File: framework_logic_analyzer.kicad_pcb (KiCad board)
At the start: 4 copper layers, 26 x 30 mm, 93 parts, among them IC1 TXU0104QWBQARQ1, IC2 TXU0104QWBQARQ1, IC3 TXU0104QWBQARQ1, IC4 TXU0104QWBQARQ1, IC5 CYUSB3014-BZXC, J1 Conn_02x08_Odd_Even, J2 Conn_02x08_Odd_Even, J3 Conn_ARM_JTAG_SWD_10, P1 USB_C_Plug, Q1 MMBT3904, Q2 MMBT3904, Q3 MMBT3904, U1 NCP360SNT1G, U2 WE-TVS-82400102, U3 AP2112K-3.3, U4 SC189CSKTRT, U5 M24M02-DR, Y1 19.200 MHz

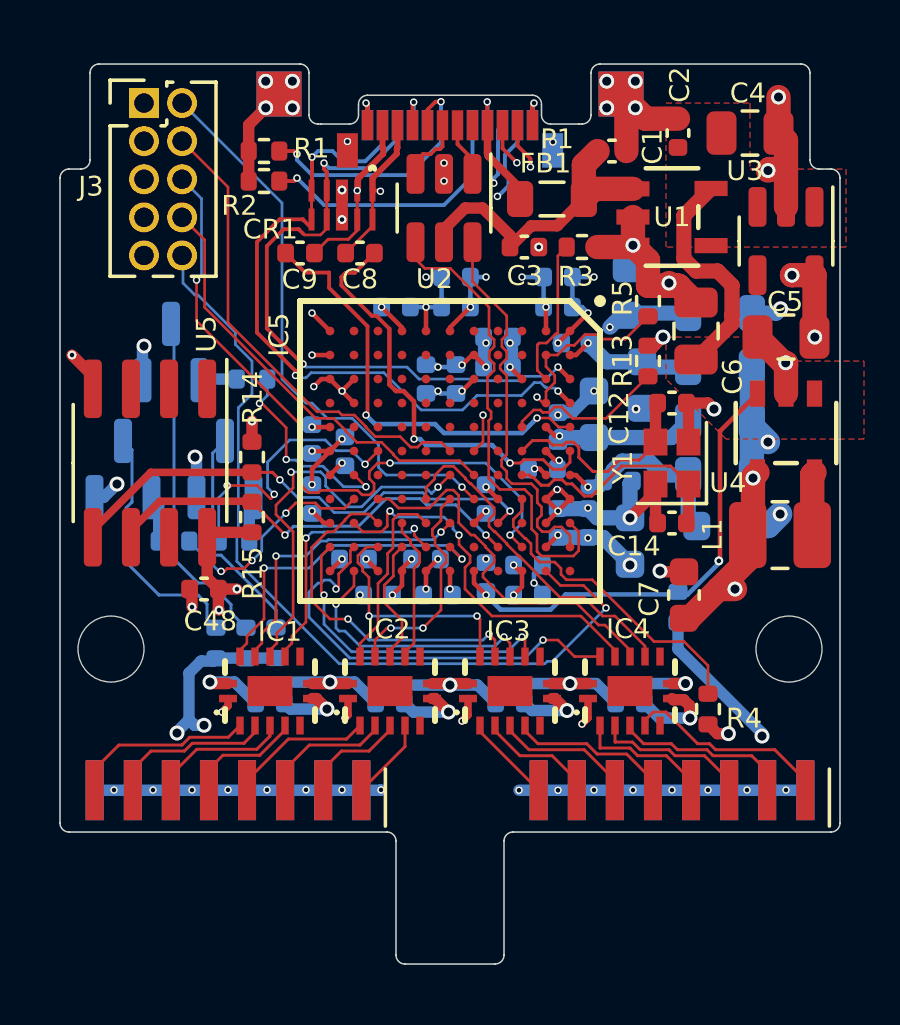
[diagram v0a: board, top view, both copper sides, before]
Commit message: update to kicad 9
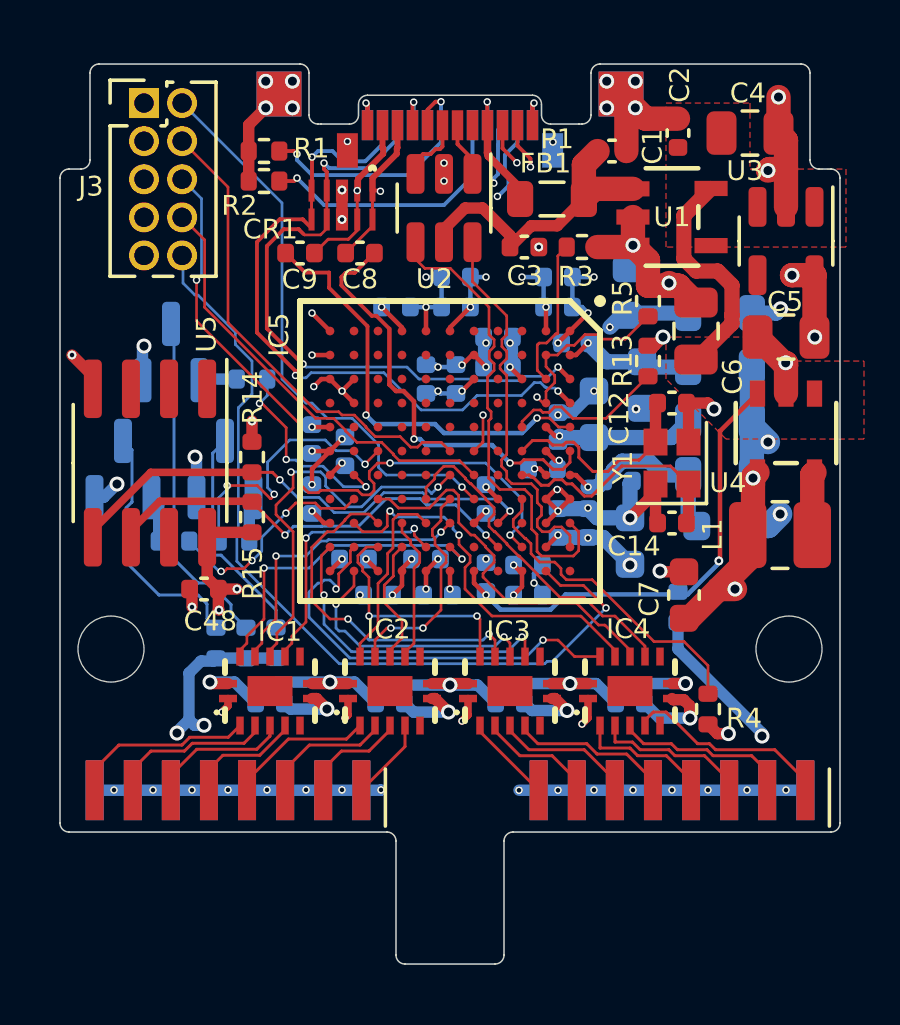
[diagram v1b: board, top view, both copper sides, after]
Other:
- outline, holes or cut-outs redrawn

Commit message: begin big refactor
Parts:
- removed J1, J2: Conn_02x08_Odd_Even, 20021311-00016T4LF:20021311-00016T4LF
- removed TP2, TP3, TP4: TestPoint, TestPoint:TestPoint_Pad_1.5x1.5mm
- added C11: 100n, Capacitor_SMD:C_0402_1005Metric, F.Cu at (154.7, 92.6)
- added C49: 100n, Capacitor_SMD:C_0402_1005Metric, F.Cu at (139.7, 92.6)
- added C50: 100n, Capacitor_SMD:C_0402_1005Metric, F.Cu at (111.7, 92.6)
- added C51: 100n, Capacitor_SMD:C_0402_1005Metric, F.Cu at (126.7, 92.6)
- added C52: 10n, Capacitor_SMD:C_0402_1005Metric, F.Cu at (110.7, 92.6)
- added C53: 10n, Capacitor_SMD:C_0402_1005Metric, F.Cu at (124.7, 92.6)
- added C54: 10n, Capacitor_SMD:C_0402_1005Metric, F.Cu at (141.7, 92.6)
- added C55: 10n, Capacitor_SMD:C_0402_1005Metric, F.Cu at (156.7, 92.6)
- added C56: 10n, Capacitor_SMD:C_0402_1005Metric, F.Cu at (156.3, 90.2)
- added C57: 10n, Capacitor_SMD:C_0402_1005Metric, F.Cu at (141.3, 89.2)
- added C58: 10n, Capacitor_SMD:C_0402_1005Metric, F.Cu at (126.3, 89.2)
- added C59: 10n, Capacitor_SMD:C_0402_1005Metric, F.Cu at (111.3, 90.2)
- added C60: 1n, Capacitor_SMD:C_0402_1005Metric, F.Cu at (126.3, 91.2)
- added C61: 1n, Capacitor_SMD:C_0402_1005Metric, F.Cu at (111.3, 91.2)
- added C62: 1n, Capacitor_SMD:C_0402_1005Metric, F.Cu at (141.3, 91.2)
- added C63: 1n, Capacitor_SMD:C_0402_1005Metric, F.Cu at (156.3, 91.2)
- added C64: 1n, Capacitor_SMD:C_0402_1005Metric, F.Cu at (109.7, 92.6)
- added C65: 1n, Capacitor_SMD:C_0402_1005Metric, F.Cu at (125.7, 92.6)
- added C66: 1n, Capacitor_SMD:C_0402_1005Metric, F.Cu at (140.7, 92.6)
- added C67: 1n, Capacitor_SMD:C_0402_1005Metric, F.Cu at (155.7, 92.6)
- added J4: 6101XX249121_610108249121, Snapeda:6101XX249121_610108249121_610108249121, F.Cu at (113.9, 104.6)
- added J5: 6101XX249121_610108249121, Snapeda:6101XX249121_610108249121_610108249121, F.Cu at (128.9, 104.6)
- added J6: 6101XX249121_610108249121, Snapeda:6101XX249121_610108249121_610108249121, F.Cu at (143.9, 104.6)
- added J7: 6101XX249121_610108249121, Snapeda:6101XX249121_610108249121_610108249121, F.Cu at (158.9, 104.6)
- C13, C15, C16, C17: moved to F.Cu
- C48, R1, R14, R15, R2, U5: moved to B.Cu
- P1: value USB_C_Plug -> USB_C_Receptacle; footprint Expansion_Card:USB_C_Plug_Molex_105444 -> Snapeda:USB4056-03-A_REVA2_GCT_USB4056-03-A_REVA2
- moved J3 55.9 mm to (175.3, 97.6), turned to -90 degrees
- moved C4 32.9 mm to (179.0, 74.9)
- moved C7 32.9 mm to (176.8, 90.3)
- moved L1 32.9 mm to (180.0, 88.3)
- moved C5 32.9 mm to (180.2, 81.7)
- moved C6 32.9 mm to (177.2, 81.5)
- moved U3 32.9 mm to (180.2, 78.5)
- moved U4 32.9 mm to (180.2, 84.9)
- moved U5 31.1 mm to (157.3, 84.7), turned to 180 degrees
- moved C2 30.7 mm to (174.3, 69.3), turned to 180 degrees
- moved U1 29.8 mm to (173.2, 71.6)
- moved R1 26.6 mm to (156.5, 74.9), turned to -90 degrees
- moved C16 26.2 mm to (156.3, 89.2), turned to 180 degrees
- moved C48 25.6 mm to (153.0, 82.3), turned to 90 degrees
- moved R2 25.5 mm to (155.1, 69.6), turned to 90 degrees
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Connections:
- net /IN0 renamed IN0
- net /IN1 renamed IN1
- net /IN10 renamed IN10
- net /IN11 renamed IN11
- net /IN12 renamed IN12
- net /IN13 renamed IN13
- net /IN14 renamed IN14
- net /IN15 renamed IN15
- net /IN2 renamed IN2
- net /IN3 renamed IN3
- net /IN4 renamed IN4
- net /IN5 renamed IN5
- net /IN6 renamed IN6
- net /IN7 renamed IN7
- net /IN8 renamed IN8
- net /IN9 renamed IN9
- CR1 pad 4: /USB-C/SS_RX- -> /USB-C/SS_RX+
- CR1 pad 5: /USB-C/SS_RX+ -> /USB-C/SS_RX-
- CR1 pad 6: /USB-C/SS_RX+ -> /USB-C/SS_RX-
- CR1 pad 7: /USB-C/SS_RX- -> /USB-C/SS_RX+
- IC1 pad 15: unconnected-(IC1-EP-Pad15) -> GND
- IC1 pad 2: /CH0 -> /Signal Input/CH0
- IC1 pad 3: /CH1 -> /Signal Input/CH1
- IC1 pad 4: /CH2 -> /Signal Input/CH2
- IC1 pad 5: /CH3 -> /Signal Input/CH3
- IC2 pad 15: unconnected-(IC2-EP-Pad15) -> GND
- IC2 pad 2: /CH4 -> /Signal Input/CH4
- IC2 pad 3: /CH5 -> /Signal Input/CH5
- IC2 pad 4: /CH6 -> /Signal Input/CH6
- IC2 pad 5: /CH7 -> /Signal Input/CH7
- IC3 pad 15: unconnected-(IC3-EP-Pad15) -> GND
- IC3 pad 2: /CH8 -> /Signal Input/CH8
- IC3 pad 3: /CH9 -> /Signal Input/CH9
- IC3 pad 4: /CH10 -> /Signal Input/CH10
- IC3 pad 5: /CH11 -> /Signal Input/CH11
- IC4 pad 15: unconnected-(IC4-EP-Pad15) -> GND
- IC4 pad 2: /CH12 -> /Signal Input/CH12
- IC4 pad 3: /CH13 -> /Signal Input/CH13
- IC4 pad 4: /CH14 -> /Signal Input/CH14
- IC4 pad 5: /CH15 -> /Signal Input/CH15
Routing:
- net GND: track 94.2 -> 61.0 mm, vias 82 -> 111
- net Net-(IC5-TRST#): track 28.4 -> 0.00 mm, vias 1 -> 0
- net /USB-C/SS_RX+: track 33.4 -> 9.89 mm, vias 4 -> 0
- net Net-(IC5-TDO): track 23.0 -> 0.00 mm, vias 3 -> 0
- net /USB-C/SS_RX-: track 30.2 -> 9.77 mm, vias 4 -> 0
- net Net-(IC5-TMS): track 19.1 -> 0.00 mm, vias 1 -> 0
- net Net-(IC5-TCK): track 16.0 -> 0.00 mm
- net VBUS: track 23.4 -> 8.38 mm, vias 2 -> 1
- net Net-(IC5-TDI): track 14.6 -> 0.00 mm
- net /USB-C/SS_TX+: track 13.4 -> 2.13 mm, vias 2 -> 0
- net +3V3: track 43.0 -> 32.7 mm, vias 23 -> 3
- net Net-(Q3-C): track 11.2 -> 1.20 mm
- net /USB-C/VBUS_IN: track 9.95 -> 0.00 mm
- net +1V2: track 20.2 -> 10.4 mm, vias 14 -> 3
- net IN11: track 10.6 -> 1.12 mm, vias 2 -> 0
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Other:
- board size 26 x 30 mm -> 63 x 40.5 mm

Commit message: more work
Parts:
- moved J3 55.0 mm to (137.2, 57.9)
- moved C7 45.6 mm to (145.6, 57.1), turned to 0 degrees
- moved L1 42.8 mm to (147.6, 60.3), turned to 90 degrees
- moved U4 38.1 mm to (151.0, 60.5), turned to 180 degrees
- moved C5 33.6 mm to (154.2, 60.5), turned to 90 degrees
- moved C6 33.1 mm to (154.4, 57.5), turned to 0 degrees
- moved U3 29.1 mm to (157.4, 60.5), turned to 180 degrees
- moved C4 23.8 mm to (161.0, 59.3), turned to -90 degrees
- moved C51 2.00 mm to (124.7, 92.6)
- moved C55 2.00 mm to (154.7, 92.6)
- moved C60 2.00 mm to (126.3, 89.2)
- moved C62 2.00 mm to (141.3, 89.2)
- moved C1 1.65 mm to (162.2, 77.0)
- moved FB1 1.65 mm to (160.2, 78.6)
- moved C3 1.65 mm to (159.2, 80.2)
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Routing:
- net GND: track 61.0 -> 106.0 mm, vias 111 -> 178
- net VIO: track 20.3 -> 43.3 mm, vias 0 -> 11
- net +3V3: track 32.7 -> 46.8 mm, vias 3 -> 15
- net IN11: track 1.12 -> 7.11 mm
- net IN8: track 9.21 -> 4.96 mm
- net IN4: track 6.91 -> 3.40 mm
- net IN14: track 12.9 -> 15.8 mm
- net IN9: track 10.2 -> 7.53 mm
- net IN15: track 11.4 -> 13.3 mm
- net IN10: track 8.36 -> 7.29 mm
- net IN5: track 6.01 -> 5.16 mm
- net IN12: track 10.3 -> 9.57 mm

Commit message: further routing
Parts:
- moved C2 29.6 mm to (144.7, 69.3), turned to 90 degrees
- moved U1 26.0 mm to (147.3, 68.8), turned to 180 degrees
- moved C6 24.2 mm to (133.8, 70.2), turned to 90 degrees
- moved L1 22.5 mm to (127.4, 70.2)
- moved U4 22.4 mm to (130.8, 70.2)
- moved C4 20.1 mm to (142.9, 68.0), turned to 90 degrees
- moved C5 19.1 mm to (136.6, 68.0)
- moved U3 19.1 mm to (139.8, 68.0)
- moved C7 18.5 mm to (130.2, 67.5)
- moved J3 18.5 mm to (122.2, 68.7)
- moved C1 14.5 mm to (149.9, 69.3), turned to 90 degrees
- moved FB1 12.3 mm to (149.8, 72.0), turned to 90 degrees
- moved TP1 9.65 mm to (120.2, 76.0)
- moved FB4 6.93 mm to (146.6, 80.8)
- moved C23 6.57 mm to (146.4, 79.1), turned to 0 degrees
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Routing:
- net GND: track 106.0 -> 146.6 mm, vias 178 -> 245
- net Net-(IC5-TRST#): track 0.00 -> 32.2 mm, vias 0 -> 1
- net Net-(IC5-TDO): track 0.00 -> 29.3 mm
- net Net-(IC5-TDI): track 0.00 -> 26.5 mm
- net Net-(IC5-TMS): track 0.00 -> 24.0 mm, vias 0 -> 1
- net Net-(IC5-TCK): track 0.00 -> 23.3 mm, vias 0 -> 1
- net IN15: track 13.3 -> 0.90 mm
- net IN14: track 15.8 -> 3.89 mm
- net +3V3: track 46.8 -> 58.3 mm, vias 15 -> 42
- net IN13: track 12.0 -> 2.40 mm
- net Net-(FB1-Pad1): track 2.46 -> 11.2 mm, vias 0 -> 4
- net /CVDDQ: track 0.00 -> 7.03 mm, vias 0 -> 1
- net IN11: track 7.11 -> 0.90 mm
- net IN12: track 9.57 -> 3.40 mm
- net IN6: track 7.71 -> 1.70 mm
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- added copper zone on F.Cu, net +1V2
- added copper zone on F.Cu, net /USB-C/VBUS_IN
- added copper zone on F.Cu, net Net-(U4-LX)
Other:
- board text added: "16 Channel Logic Analyzer June 2025 Rev 0.1"
- board text added: "RST DI DO CK MS"
- board text removed: "April 2023"
- board text removed: "Framework Logic Analyzer"
- board text removed: "Jack LeFevre"
- board text removed: "Rev.0"

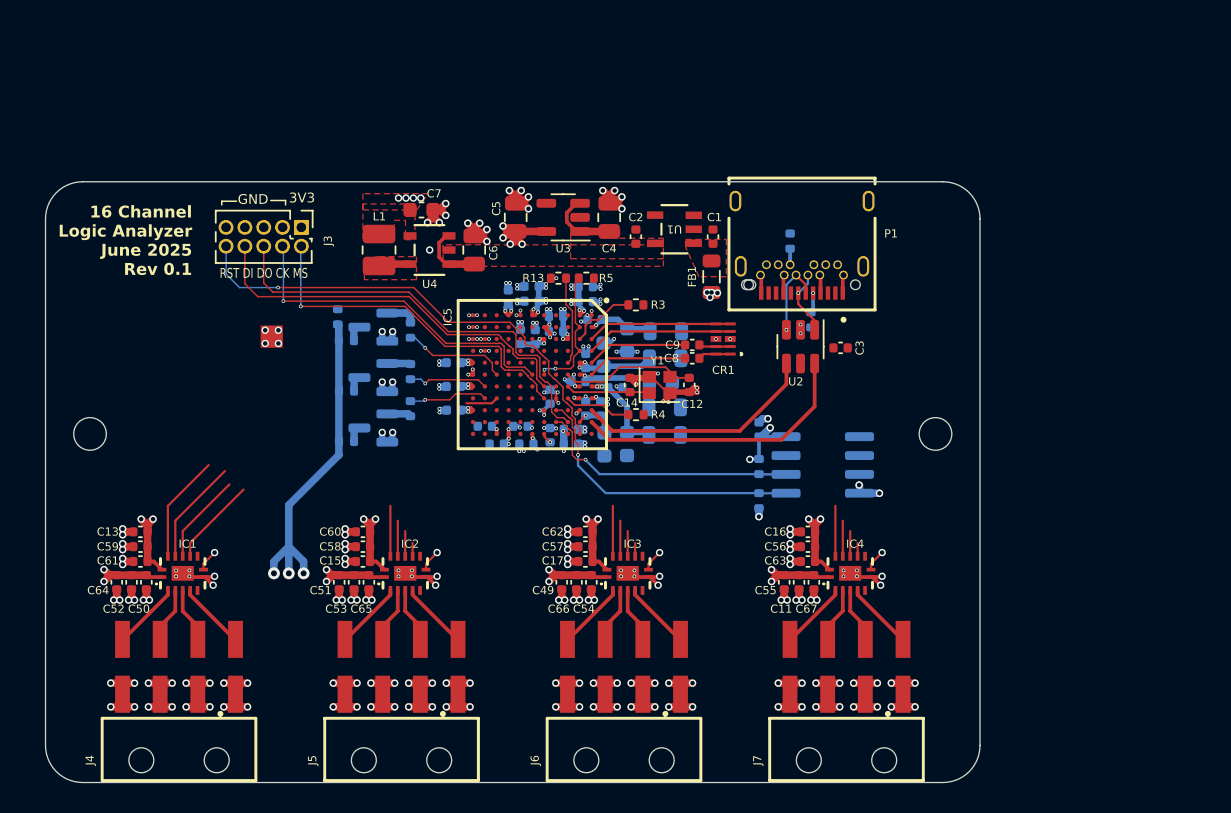
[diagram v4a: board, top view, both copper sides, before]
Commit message: more routing, add differential pair netclass
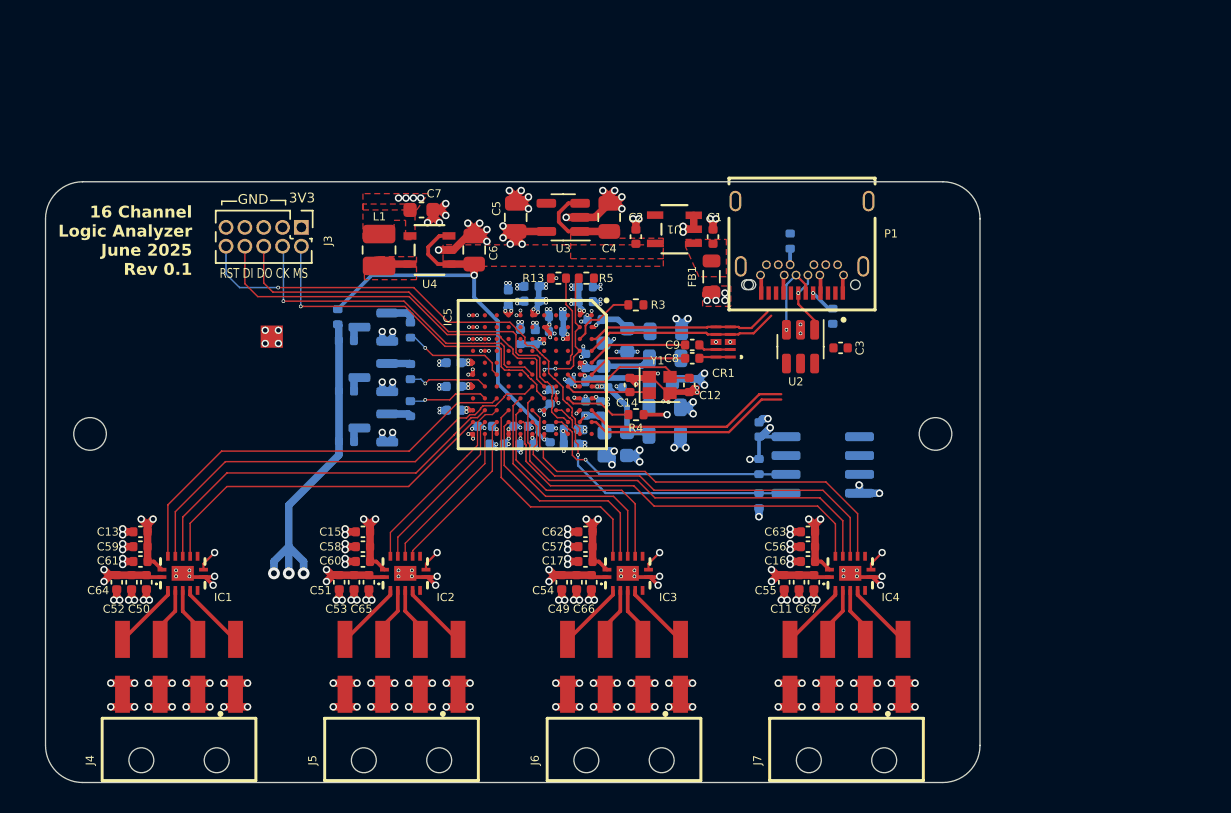
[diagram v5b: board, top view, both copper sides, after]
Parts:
- moved C15 2.00 mm to (126.3, 89.2)
- moved C16 2.00 mm to (156.3, 91.2)
- moved C54 2.00 mm to (139.7, 92.6)
- moved C60 2.00 mm to (126.3, 91.2)
- moved C63 2.00 mm to (156.3, 89.2)
- moved R1 1.49 mm to (158.0, 74.7)
- moved C49 1.00 mm to (140.7, 92.6)
- moved C66 1.00 mm to (141.7, 92.6)
- moved CR1 0.20 mm to (150.6, 76.4)
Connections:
- IC5 pad F10: IN0 -> IN14
- IC5 pad F7: IN2 -> IN1
- IC5 pad F8: IN5 -> IN13
- IC5 pad F9: IN1 -> IN15
- IC5 pad G10: IN3 -> IN12
- IC5 pad G8: IN15 -> IN10
- IC5 pad G9: IN4 -> IN11
- IC5 pad H10: IN6 -> IN9
- IC5 pad H9: IN7 -> IN8
- IC5 pad J10: IN8 -> IN7
- IC5 pad J8: IN14 -> IN0
- IC5 pad J9: IN9 -> IN4
- IC5 pad K10: IN12 -> IN5
- IC5 pad K11: IN10 -> IN6
- IC5 pad K9: IN13 -> IN2
- IC5 pad L10: IN11 -> IN3
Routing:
- net IN15: track 0.90 -> 29.1 mm
- net IN13: track 2.40 -> 29.6 mm
- net VBUS: track 10.0 -> 36.8 mm, vias 1 -> 2
- net IN12: track 3.40 -> 27.7 mm
- net IN14: track 3.89 -> 28.1 mm
- net IN1: track 7.14 -> 30.6 mm
- net GND: track 146.6 -> 168.6 mm, vias 245 -> 266
- net IN0: track 7.29 -> 28.6 mm
- net IN2: track 6.15 -> 26.0 mm
- net IN3: track 5.99 -> 24.1 mm
- net IN11: track 0.90 -> 16.3 mm
- net IN10: track 1.70 -> 16.7 mm
- net IN9: track 2.40 -> 15.1 mm
- net IN8: track 3.40 -> 15.9 mm
- net IN7: track 0.90 -> 11.4 mm
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- added copper zone on F.Cu, net Net-(FB1-Pad1)

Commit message: length match input channels
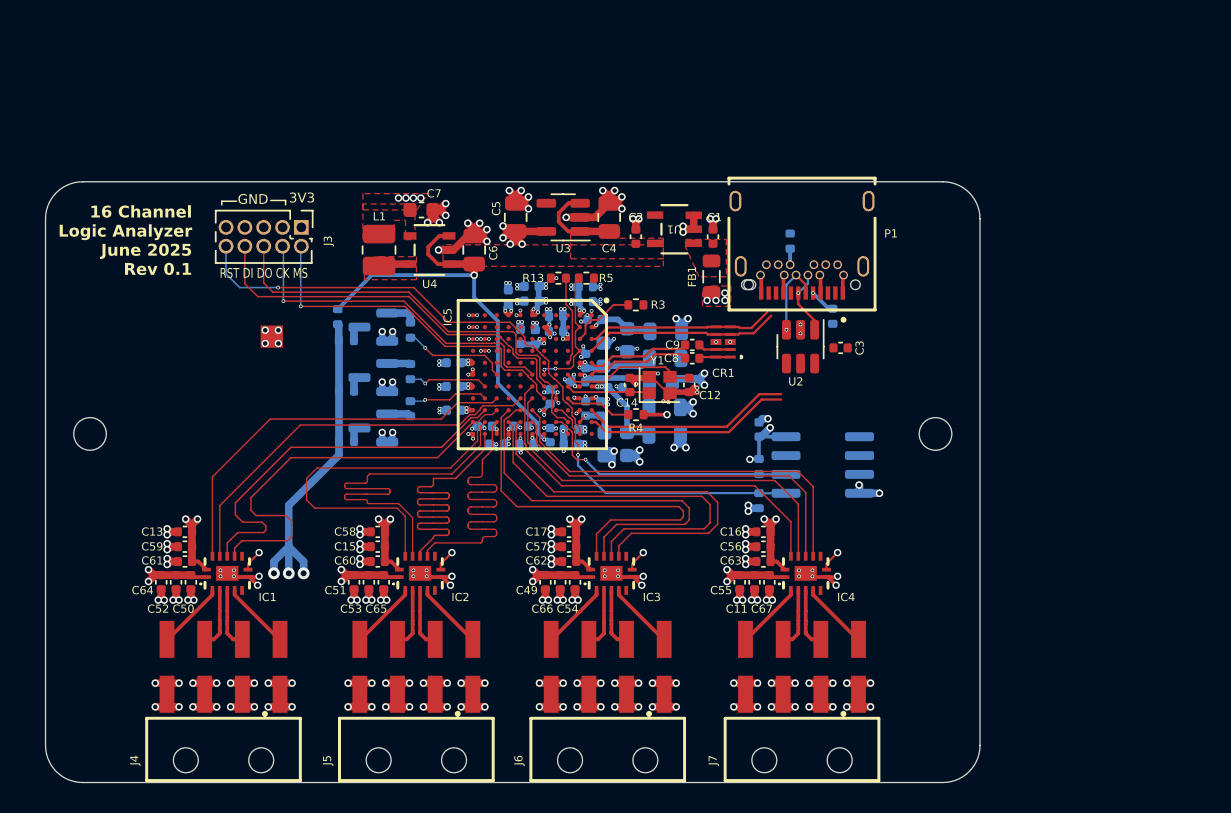
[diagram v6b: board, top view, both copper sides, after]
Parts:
- moved C16 3.61 mm to (153.3, 89.2)
- moved C63 3.61 mm to (153.3, 91.2)
- moved C11 3.00 mm to (152.7, 92.6)
- moved C13 3.00 mm to (114.3, 89.2)
- moved C50 3.00 mm to (114.7, 92.6)
- moved C52 3.00 mm to (113.7, 92.6)
- moved C55 3.00 mm to (151.7, 92.6)
- moved C56 3.00 mm to (153.3, 90.2)
- moved C59 3.00 mm to (114.3, 90.2)
- moved C61 3.00 mm to (114.3, 91.2)
- moved C64 3.00 mm to (112.7, 92.6)
- moved C67 3.00 mm to (153.7, 92.6)
- moved IC1 3.00 mm to (117.2, 92.0)
- moved IC4 3.00 mm to (156.2, 92.0)
- moved J4 3.00 mm to (116.9, 104.6)
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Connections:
- net Net-(IC5-SSTXM) renamed /SS_AC_TX-
- net Net-(IC5-SSTXP) renamed /SS_AC_TX+
- IC5 pad F7: IN1 -> IN12
- IC5 pad G10: IN12 -> IN11
- IC5 pad G8: IN10 -> IN1
- IC5 pad G9: IN11 -> IN9
- IC5 pad H10: IN9 -> IN10
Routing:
- net IN6: track 10.5 -> 26.6 mm
- net IN5: track 11.5 -> 26.7 mm
- net IN7: track 11.4 -> 26.6 mm
- net IN4: track 13.1 -> 26.7 mm
- net IN9: track 15.1 -> 26.7 mm
- net IN8: track 15.9 -> 26.7 mm
- net IN11: track 16.3 -> 26.7 mm
- net IN10: track 16.7 -> 26.7 mm
- net +3V3: track 60.2 -> 65.2 mm, vias 44 -> 45
- net IN1: track 30.6 -> 26.7 mm
- net IN13: track 29.6 -> 26.7 mm
- net IN14: track 28.1 -> 25.4 mm
- net IN3: track 24.1 -> 26.7 mm
- net IN15: track 29.1 -> 26.7 mm
- net IN0: track 28.6 -> 26.7 mm
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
